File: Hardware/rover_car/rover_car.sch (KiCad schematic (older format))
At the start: 26 parts, among them J1 Conn_01x06_Female, J3 Screw_Terminal_01x02, M1 Motor_DC, M2 Motor_DC, M3 Motor_DC, M4 Motor_DC, M5 Motor_DC, M6 Motor_DC, U1 DRV8833PWP, U2 DRV8833PWP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

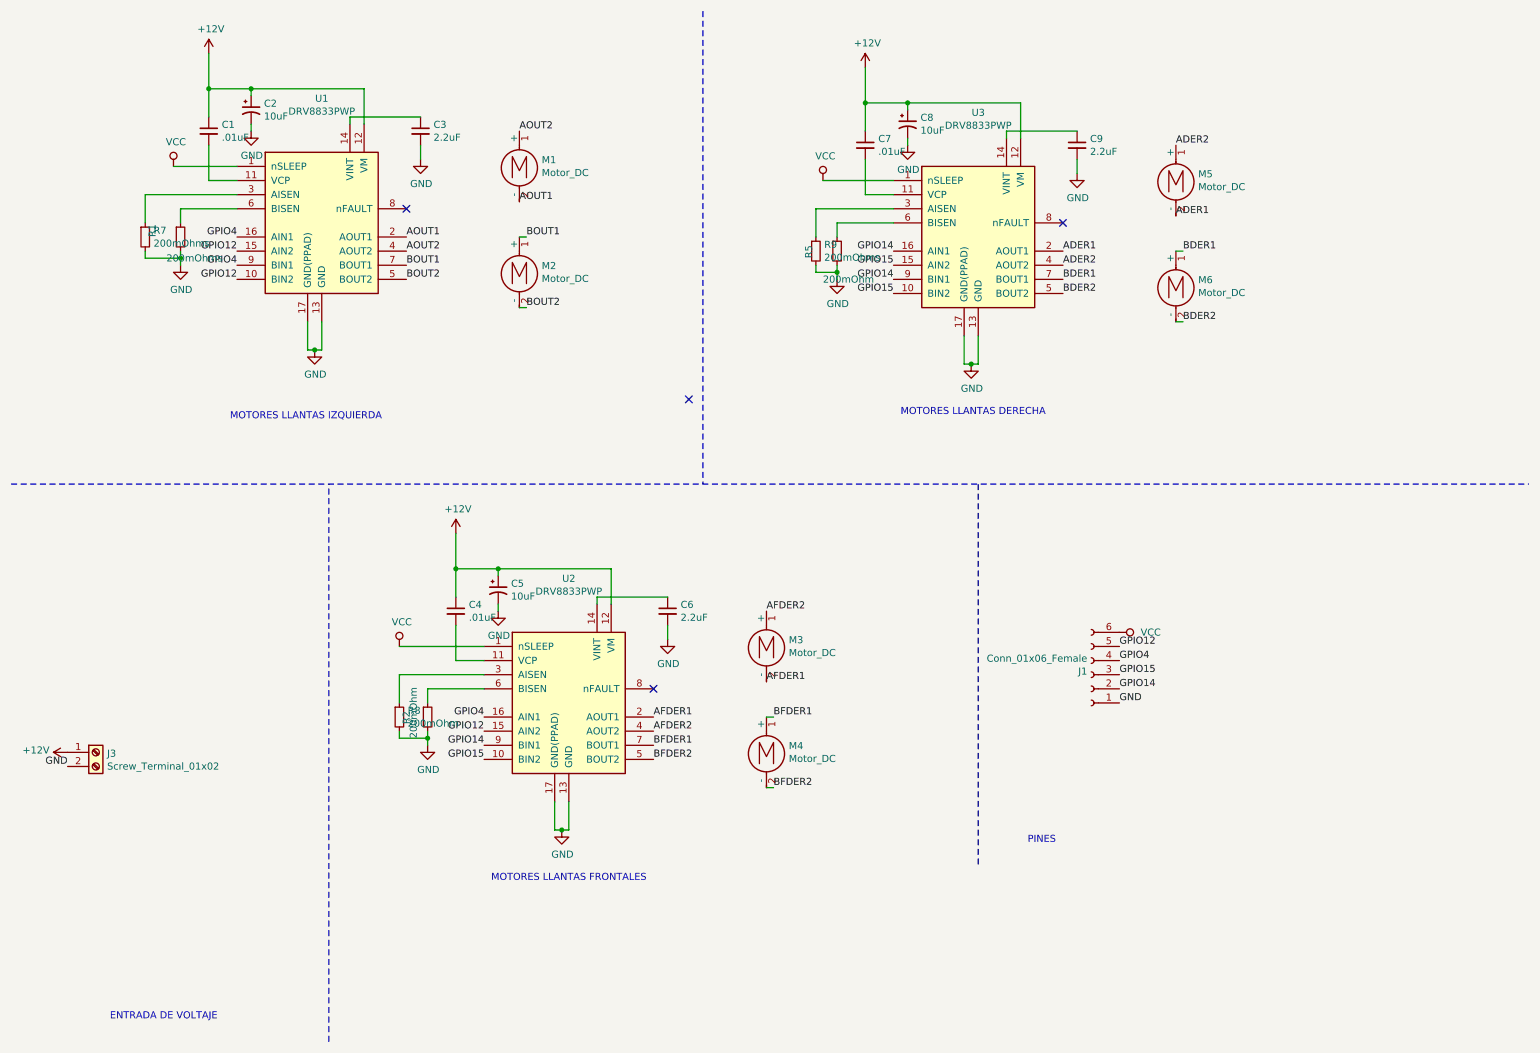
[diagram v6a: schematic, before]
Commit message: fix corners
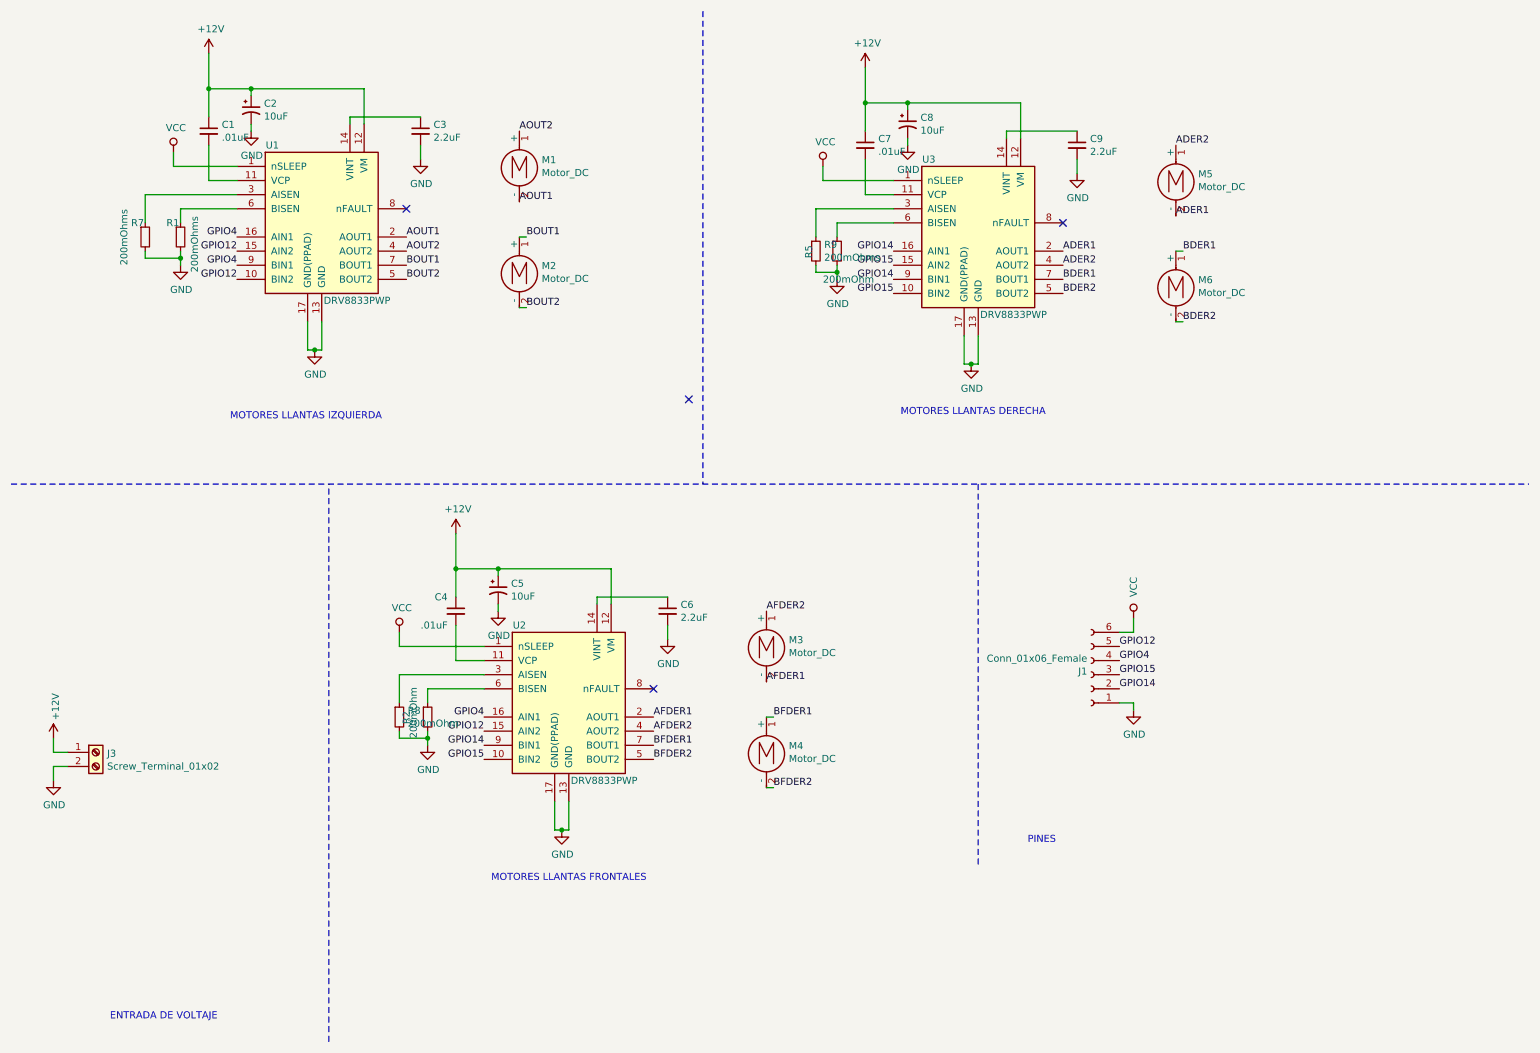
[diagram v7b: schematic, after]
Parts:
- C7: manf# 710-885012207039 -> 885012207039
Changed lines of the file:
@@
 U 1 1 5D1E7C75
 P 1650 2100
-F 0 "R1" V 1450 2100 50  0000 L CNN
-F 1 "200mOhms" H 1550 1950 50  0000 L CNN
+F 0 "R1" H 1550 2200 50  0000 L CNN
+F 1 "200mOhms" V 1750 1850 50  0000 L CNN
 F 2 "Resistor_SMD:R_0805_2012Metric_Pad1.15x1.40mm_HandSolder" H 1650 2100 50  0001 C CNN
 F 3 "https://www.mouser.mx/datasheet/2/315/AOA0000C334-1314047.pdf" H 1650 2100 50  0001 C CNN
@@
 F 2 "Capacitor_SMD:C_0805_2012Metric_Pad1.15x1.40mm_HandSolder" H 6500 1450 50  0001 C CNN
 F 3 "https://www.mouser.mx/datasheet/2/445/885012207039-554525.pdf" H 6500 1450 50  0001 C CNN
-F 4 "710-885012207039" H 6500 1450 50  0001 C CNN "manf#"
+F 4 "885012207039" H 6500 1450 50  0001 C CNN "manf#"
 	1    6500 1450
 	1    0    0    -1
@@
 U 1 1 5D1F7EB7
 P 7300 2100
-F 0 "U3" H 7300 2981 50  0000 C CNN
-F 1 "DRV8833PWP" H 7300 2890 50  0000 C CNN
+F 0 "U3" H 6950 2650 50  0000 C CNN
+F 1 "DRV8833PWP" H 7550 1550 50  0000 C CNN
 F 2 "Package_SO:HTSSOP-16-1EP_4.4x5mm_P0.65mm_EP3.4x5mm_Mask2.46x2.31mm_ThermalVias" H 7750 2550 50  0001 L CNN
 F 3 "http://www.ti.com/lit/ds/symlink/drv8833.pdf" H 7150 2650 50  0001 C CNN
@@
 U 1 1 5D21617C
 P 3600 4750
-F 0 "C4" H 3692 4796 50  0000 L CNN
-F 1 ".01uF" H 3692 4705 50  0000 L CNN
+F 0 "C4" H 3450 4850 50  0000 L CNN
+F 1 ".01uF" H 3350 4650 50  0000 L CNN
 F 2 "Capacitor_SMD:C_0805_2012Metric_Pad1.15x1.40mm_HandSolder" H 3600 4750 50  0001 C CNN
 F 3 "https://www.mouser.mx/datasheet/2/445/885012207039-554525.pdf" H 3600 4750 50  0001 C CNN
@@
 U 1 1 5D21620A
 P 4400 5400
-F 0 "U2" H 4400 6281 50  0000 C CNN
-F 1 "DRV8833PWP" H 4400 6190 50  0000 C CNN
+F 0 "U2" H 4050 5950 50  0000 C CNN
+F 1 "DRV8833PWP" H 4650 4850 50  0000 C CNN
 F 2 "Package_SO:HTSSOP-16-1EP_4.4x5mm_P0.65mm_EP3.4x5mm_Mask2.46x2.31mm_ThermalVias" H 4850 5850 50  0001 L CNN
 F 3 "http://www.ti.com/lit/ds/symlink/drv8833.pdf" H 4250 5950 50  0001 C CNN
@@
 Text Label 5000 5800 0    50   ~ 0
 BFDER2
-Text Label 8300 5400 0    50   ~ 0
-GND
 $Comp
 L power:+12V #PWR02
@@
 	1    0    0    -1
 $EndComp
-Text Label 850  5850 2    50   ~ 0
-GND
 $Comp
 L power:+12V #PWR08
 U 1 1 5D237185
-P 850 5750
-F 0 "#PWR08" H 850 5600 50  0001 C CNN
-F 1 "+12V" V 865 5878 50  0000 L CNN
-F 2 "" H 850 5750 50  0001 C CNN
-F 3 "" H 850 5750 50  0001 C CNN
-	1    850  5750
-	0    -1   -1   0
+P 750 5650
+F 0 "#PWR08" H 750 5500 50  0001 C CNN
+F 1 "+12V" V 765 5778 50  0000 L CNN
+F 2 "" H 750 5650 50  0001 C CNN
+F 3 "" H 750 5650 50  0001 C CNN
+	1    750  5650
+	1    0    0    -1
 $EndComp
 $Comp
@@
 L power:VCC #PWR0106
 U 1 1 5D27DD7D
-P 8300 4900
-F 0 "#PWR0106" H 8300 4750 50  0001 C CNN
-F 1 "VCC" V 8300 5050 50  0000 L CNN
-F 2 "" H 8300 4900 50  0001 C CNN
-F 3 "" H 8300 4900 50  0001 C CNN
-	1    8300 4900
-	0    1    1    0
+P 8400 4800
+F 0 "#PWR0106" H 8400 4650 50  0001 C CNN
+F 1 "VCC" V 8400 4950 50  0000 L CNN
+F 2 "" H 8400 4800 50  0001 C CNN
+F 3 "" H 8400 4800 50  0001 C CNN
+	1    8400 4800
+	1    0    0    -1
 $EndComp
 $Comp
@@
 U 1 1 5D250BC0
 P 1400 2100
-F 0 "R7" H 1459 2146 50  0000 L CNN
-F 1 "200mOhms" H 1459 2055 50  0000 L CNN
+F 0 "R7" H 1300 2200 50  0000 L CNN
+F 1 "200mOhms" V 1250 1900 50  0000 L CNN
 F 2 "Resistor_SMD:R_0805_2012Metric_Pad1.15x1.40mm_HandSolder" H 1400 2100 50  0001 C CNN
 F 3 "~" H 1400 2100 50  0001 C CNN
@@
 L power:VCC #PWR0101
 U 1 1 5D3268F3
-P 1600 1600
-F 0 "#PWR0101" H 1600 1450 50  0001 C CNN
-F 1 "VCC" H 1617 1773 50  0000 C CNN
-F 2 "" H 1600 1600 50  0001 C CNN
-F 3 "" H 1600 1600 50  0001 C CNN
-	1    1600 1600
+P 1600 1500
+F 0 "#PWR0101" H 1600 1350 50  0001 C CNN
+F 1 "VCC" H 1617 1673 50  0000 C CNN
+F 2 "" H 1600 1500 50  0001 C CNN
+F 3 "" H 1600 1500 50  0001 C CNN
+	1    1600 1500
 	1    0    0    -1
 $EndComp
@@
 U 1 1 5D1CE3C8
 P 2650 2000
-F 0 "U1" H 2650 2881 50  0000 C CNN
-F 1 "DRV8833PWP" H 2650 2790 50  0000 C CNN
+F 0 "U1" H 2300 2550 50  0000 C CNN
+F 1 "DRV8833PWP" H 2900 1450 50  0000 C CNN
 F 2 "Package_SO:HTSSOP-16-1EP_4.4x5mm_P0.65mm_EP3.4x5mm_Mask2.46x2.31mm_ThermalVias" H 3100 2450 50  0001 L CNN
 F 3 "http://www.ti.com/lit/ds/symlink/drv8833.pdf" H 2500 2550 50  0001 C CNN
@@
 L power:VCC #PWR0102
 U 1 1 5D3276DD
-P 6200 1700
-F 0 "#PWR0102" H 6200 1550 50  0001 C CNN
-F 1 "VCC" H 6217 1873 50  0000 C CNN
-F 2 "" H 6200 1700 50  0001 C CNN
-F 3 "" H 6200 1700 50  0001 C CNN
-	1    6200 1700
+P 6200 1600
+F 0 "#PWR0102" H 6200 1450 50  0001 C CNN
+F 1 "VCC" H 6217 1773 50  0000 C CNN
+F 2 "" H 6200 1600 50  0001 C CNN
+F 3 "" H 6200 1600 50  0001 C CNN
+	1    6200 1600
 	1    0    0    -1
 $EndComp
@@
 L power:VCC #PWR0103
 U 1 1 5D32E8F4
-P 3200 5000
-F 0 "#PWR0103" H 3200 4850 50  0001 C CNN
-F 1 "VCC" H 3217 5173 50  0000 C CNN
-F 2 "" H 3200 5000 50  0001 C CNN
-F 3 "" H 3200 5000 50  0001 C CNN
-	1    3200 5000
+P 3200 4900
+F 0 "#PWR0103" H 3200 4750 50  0001 C CNN
+F 1 "VCC" H 3217 5073 50  0000 C CNN
+F 2 "" H 3200 4900 50  0001 C CNN
+F 3 "" H 3200 4900 50  0001 C CNN
+	1    3200 4900
 	1    0    0    -1
 $EndComp
@@
 NoConn ~ 5000 5300
 NoConn ~ 5250 3250
+Wire Wire Line
+	750  5650 750  5750
+Wire Wire Line
+	750  5750 850  5750
+$Comp
+L power:GND #PWR0107
+U 1 1 5D44F19F
+P 750 5950
+F 0 "#PWR0107" H 750 5700 50  0001 C CNN
+F 1 "GND" H 755 5777 50  0000 C CNN
+F 2 "" H 750 5950 50  0001 C CNN
+F 3 "" H 750 5950 50  0001 C CNN
+	1    750  5950
+	1    0    0    -1
+$EndComp
+Wire Wire Line
+	850  5850 750  5850
+Wire Wire Line
+	750  5850 750  5950
+$Comp
+L power:GND #PWR0108
+U 1 1 5D453D33
+P 8400 5450
+F 0 "#PWR0108" H 8400 5200 50  0001 C CNN
+F 1 "GND" H 8405 5277 50  0000 C CNN
+F 2 "" H 8400 5450 50  0001 C CNN
+F 3 "" H 8400 5450 50  0001 C CNN
+	1    8400 5450
+	1    0    0    -1
+$EndComp
+Wire Wire Line
+	8400 5450 8400 5400
+Wire Wire Line
+	8400 5400 8300 5400
+Wire Wire Line
+	8400 4800 8400 4900
+Wire Wire Line
+	8400 4900 8300 4900
+Wire Wire Line
+	6200 1600 6200 1700
+Wire Wire Line
+	3200 4900 3200 5000
+Wire Wire Line
+	1600 1500 1600 1600
 $EndSCHEMATC

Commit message: Fix component number and etching
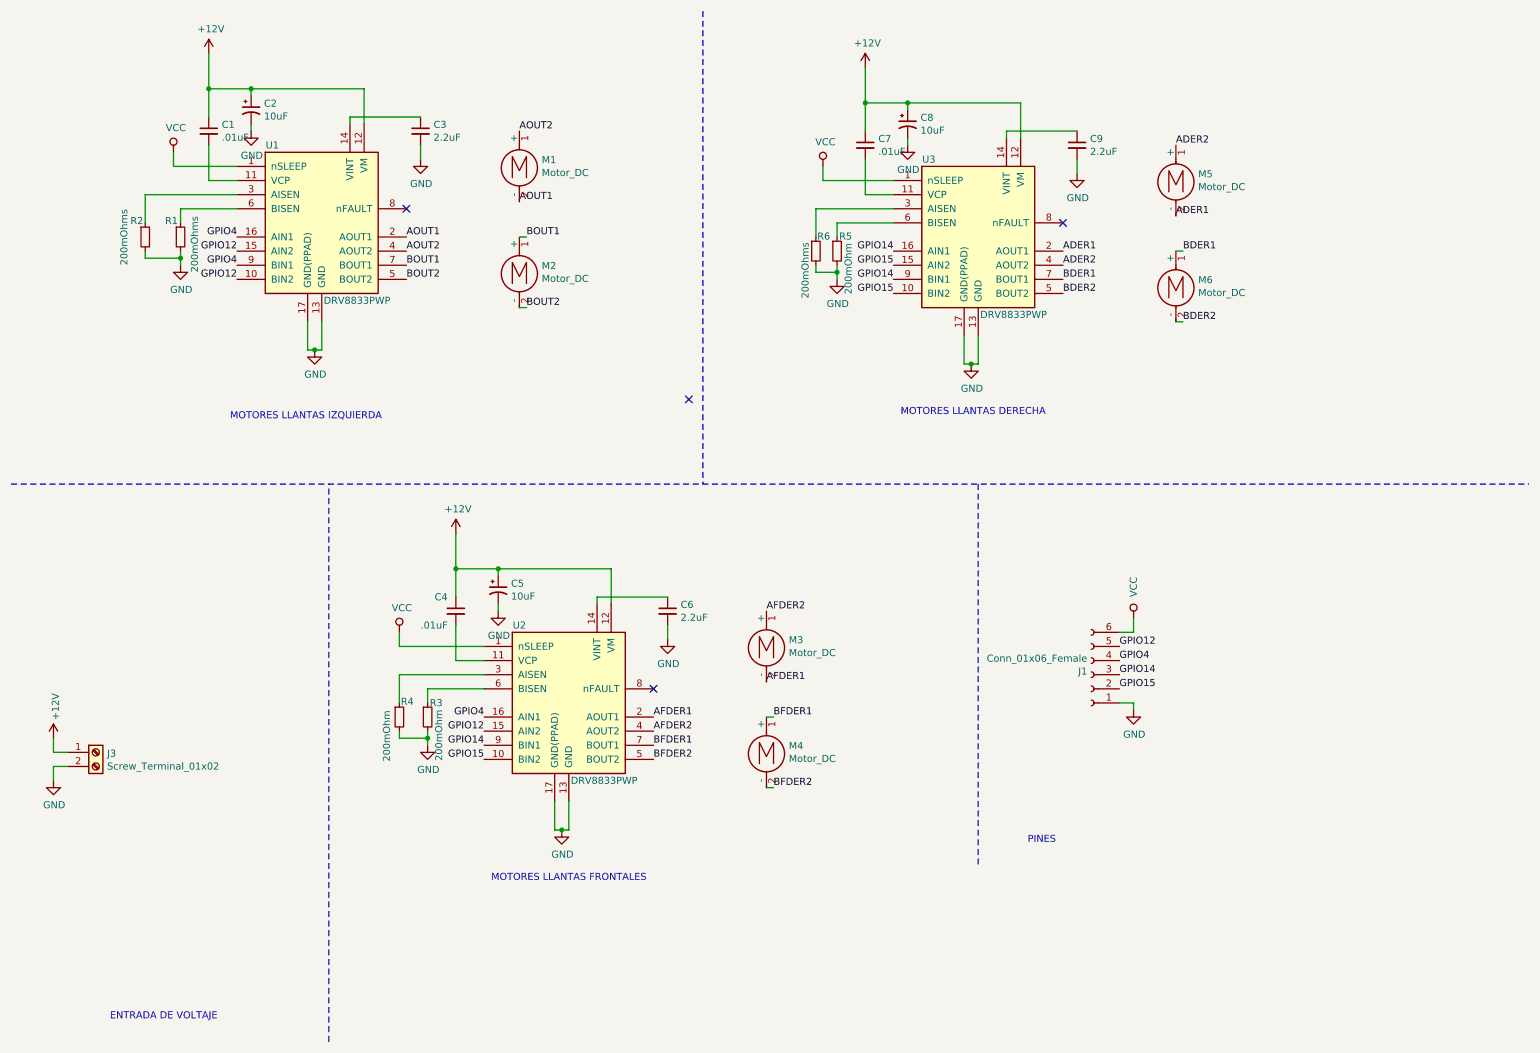
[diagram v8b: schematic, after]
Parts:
- C5: footprint Capacitor_SMD:C_Elec_4x5.4 -> Capacitor_SMD:CP_Elec_4x5.4
- renumbered R7 to R2, R2 to R3, R8 to R4, R9 to R6
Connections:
- net GPIO14: now also J1.3 (Pin_3); no longer J1.2 (Pin_2)
- net GPIO15: now also J1.2 (Pin_2); no longer J1.3 (Pin_3)
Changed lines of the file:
@@
 U 1 1 5D1E7C75
 P 1650 2100
-F 0 "R1" H 1550 2200 50  0000 L CNN
+F 0 "R1" H 1540 2215 50  0000 L CNN
 F 1 "200mOhms" V 1750 1850 50  0000 L CNN
 F 2 "Resistor_SMD:R_0805_2012Metric_Pad1.15x1.40mm_HandSolder" H 1650 2100 50  0001 C CNN
@@
 U 1 1 5D1F7E9A
 P 6300 2200
-F 0 "R5" V 6100 2150 50  0000 L CNN
-F 1 "200mOhm" H 6200 2000 50  0000 L CNN
+F 0 "R5" H 6315 2305 50  0000 L CNN
+F 1 "200mOhm" V 6380 1895 50  0000 L CNN
 F 2 "Resistor_SMD:R_0805_2012Metric_Pad1.15x1.40mm_HandSolder" H 6300 2200 50  0001 C CNN
 F 3 "https://www.mouser.mx/datasheet/2/315/AOA0000C334-1314047.pdf" H 6300 2200 50  0001 C CNN
@@
 Text Label 3250 2400 0    50   ~ 0
 BOUT2
+Text Label 8300 5200 0    50   ~ 0
+GPIO14
 Text Label 8300 5300 0    50   ~ 0
-GPIO14
-Text Label 8300 5200 0    50   ~ 0
 GPIO15
 $Comp
@@
 F 0 "C5" H 3991 4646 50  0000 L CNN
 F 1 "10uF" H 3991 4555 50  0000 L CNN
-F 2 "Capacitor_SMD:C_Elec_4x5.4" H 3900 4600 50  0001 C CNN
+F 2 "Capacitor_SMD:CP_Elec_4x5.4" H 3900 4600 50  0001 C CNN
 F 3 "https://katalog.we-online.de/pbs/datasheet/865090440003.pdf" H 3900 4600 50  0001 C CNN
 F 4 "865090440003	" H 3900 4600 50  0001 C CNN "manf#"
@@
 	5850 6000 5800 6000
 $Comp
-L Device:R_Small R2
+L Device:R_Small R3
 U 1 1 5D2161EF
 P 3400 5500
-F 0 "R2" V 3250 5450 50  0000 L CNN
-F 1 "200mOhm" V 3300 5350 50  0000 L CNN
+F 0 "R3" H 3415 5600 50  0000 L CNN
+F 1 "200mOhm" V 3480 5190 50  0000 L CNN
 F 2 "Resistor_SMD:R_0805_2012Metric_Pad1.15x1.40mm_HandSolder" H 3400 5500 50  0001 C CNN
 F 3 "https://www.mouser.mx/datasheet/2/315/AOA0000C334-1314047.pdf" H 3400 5500 50  0001 C CNN
@@
 $EndComp
 $Comp
-L Device:R_Small R7
+L Device:R_Small R2
 U 1 1 5D250BC0
 P 1400 2100
-F 0 "R7" H 1300 2200 50  0000 L CNN
+F 0 "R2" H 1295 2215 50  0000 L CNN
 F 1 "200mOhms" V 1250 1900 50  0000 L CNN
 F 2 "Resistor_SMD:R_0805_2012Metric_Pad1.15x1.40mm_HandSolder" H 1400 2100 50  0001 C CNN
@@
 $EndComp
 $Comp
-L Device:R_Small R9
+L Device:R_Small R6
 U 1 1 5D251635
 P 6150 2200
-F 0 "R9" H 6209 2246 50  0000 L CNN
-F 1 "200mOhms" H 6209 2155 50  0000 L CNN
+F 0 "R6" H 6160 2305 50  0000 L CNN
+F 1 "200mOhms" V 6075 1865 50  0000 L CNN
 F 2 "Resistor_SMD:R_0805_2012Metric_Pad1.15x1.40mm_HandSolder" H 6150 2200 50  0001 C CNN
 F 3 "~" H 6150 2200 50  0001 C CNN
@@
 	1650 2250 1650 2300
 $Comp
-L Device:R_Small R8
+L Device:R_Small R4
 U 1 1 5D258DA4
 P 3200 5500
-F 0 "R8" H 3259 5546 50  0000 L CNN
-F 1 "200mOhm" H 3259 5455 50  0000 L CNN
+F 0 "R4" H 3210 5610 50  0000 L CNN
+F 1 "200mOhm" V 3110 5185 50  0000 L CNN
 F 2 "Resistor_SMD:R_0805_2012Metric_Pad1.15x1.40mm_HandSolder" H 3200 5500 50  0001 C CNN
 F 3 "~" H 3200 5500 50  0001 C CNN
